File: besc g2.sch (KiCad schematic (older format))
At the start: 7 parts

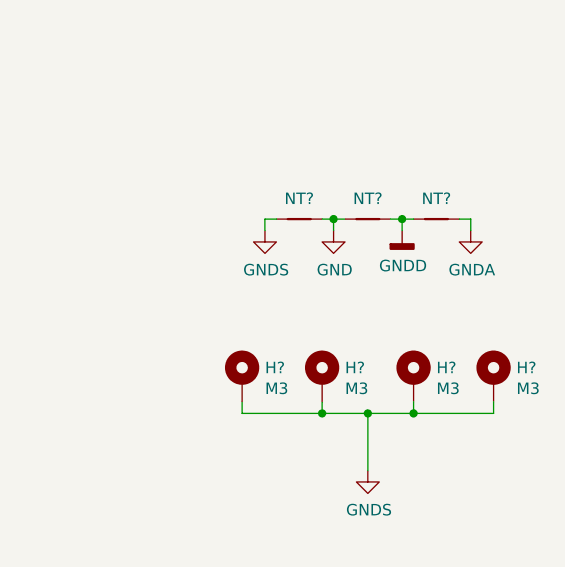
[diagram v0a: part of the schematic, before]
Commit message: power stage layout draft
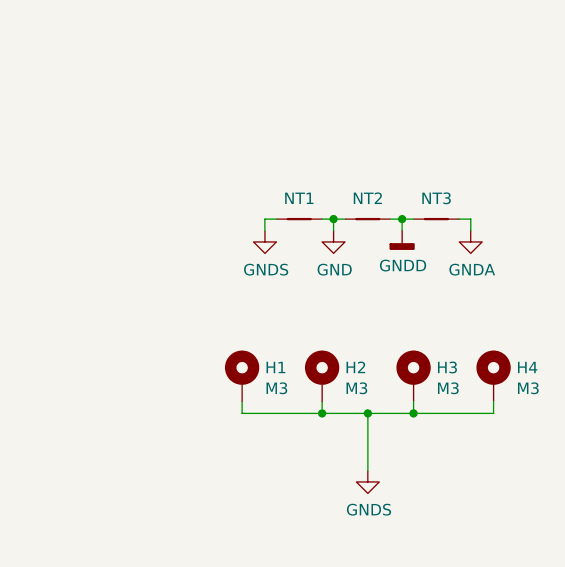
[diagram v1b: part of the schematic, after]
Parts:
- H1, H2, H3, H4: renamed from H?; footprint (none) -> MountingHole:MountingHole_3.2mm_M3_Pad_Via
- NT1, NT2, NT3: renamed from NT?; footprint (none) -> NetTie:NetTie-2_THT_Pad1.0mm
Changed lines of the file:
@@
 P 10150 3350
 AR Path="/5CA11DF8/5CEB744C" Ref="#PWR?"  Part="1"
-AR Path="/5CEB744C" Ref="#PWR0101"  Part="1"
-F 0 "#PWR0101" H 10150 3100 50  0001 C CNN
+AR Path="/5CEB744C" Ref="#PWR05"  Part="1"
+F 0 "#PWR05" H 10150 3100 50  0001 C CNN
 F 1 "GNDA" H 10155 3177 50  0000 C CNN
 F 2 "" H 10150 3350 50  0001 C CNN
@@
 $EndSheet
 $Comp
-L Device:Net-Tie_2 NT?
+L Device:Net-Tie_2 NT2
 U 1 1 5D34A5B5
 P 9700 3300
-F 0 "NT?" H 9700 3389 50  0000 C CNN
+F 0 "NT2" H 9700 3389 50  0000 C CNN
 F 1 "nt" H 9700 3390 50  0001 C CNN
-F 2 "" H 9700 3300 50  0001 C CNN
+F 2 "NetTie:NetTie-2_THT_Pad1.0mm" H 9700 3300 50  0001 C CNN
 F 3 "~" H 9700 3300 50  0001 C CNN
 	1    9700 3300
@@
 $EndComp
 $Comp
-L Device:Net-Tie_2 NT?
+L Device:Net-Tie_2 NT3
 U 1 1 5D34B582
 P 10000 3300
-F 0 "NT?" H 10000 3389 50  0000 C CNN
+F 0 "NT3" H 10000 3389 50  0000 C CNN
 F 1 "nt" H 10000 3390 50  0001 C CNN
-F 2 "" H 10000 3300 50  0001 C CNN
+F 2 "NetTie:NetTie-2_THT_Pad1.0mm" H 10000 3300 50  0001 C CNN
 F 3 "~" H 10000 3300 50  0001 C CNN
 	1    10000 3300
@@
 P 9850 3350
 AR Path="/5CA11DF8/5CEB7446" Ref="#PWR?"  Part="1"
-AR Path="/5CEB7446" Ref="#PWR0102"  Part="1"
-F 0 "#PWR0102" H 9850 3100 50  0001 C CNN
+AR Path="/5CEB7446" Ref="#PWR04"  Part="1"
+F 0 "#PWR04" H 9850 3100 50  0001 C CNN
 F 1 "GNDD" H 9854 3195 50  0000 C CNN
 F 2 "" H 9850 3350 50  0001 C CNN
@@
 P 9550 3350
 AR Path="/5CA11DF8/5CEB7455" Ref="#PWR?"  Part="1"
-AR Path="/5CEB7455" Ref="#PWR0103"  Part="1"
-F 0 "#PWR0103" H 9550 3100 50  0001 C CNN
+AR Path="/5CEB7455" Ref="#PWR02"  Part="1"
+F 0 "#PWR02" H 9550 3100 50  0001 C CNN
 F 1 "GND" H 9555 3177 50  0000 C CNN
 F 2 "" H 9550 3350 50  0001 C CNN
@@
 $EndComp
 $Comp
-L Mechanical:MountingHole_Pad H?
+L Mechanical:MountingHole_Pad H2
 U 1 1 5DC1CF77
 P 9500 4000
-F 0 "H?" H 9600 4049 50  0000 L CNN
+F 0 "H2" H 9600 4049 50  0000 L CNN
 F 1 "M3" H 9600 3958 50  0000 L CNN
-F 2 "" H 9500 4000 50  0001 C CNN
+F 2 "MountingHole:MountingHole_3.2mm_M3_Pad_Via" H 9500 4000 50  0001 C CNN
 F 3 "~" H 9500 4000 50  0001 C CNN
 	1    9500 4000
@@
 $EndComp
 $Comp
-L Mechanical:MountingHole_Pad H?
+L Mechanical:MountingHole_Pad H3
 U 1 1 5DC1D147
 P 9900 4000
-F 0 "H?" H 10000 4049 50  0000 L CNN
+F 0 "H3" H 10000 4049 50  0000 L CNN
 F 1 "M3" H 10000 3958 50  0000 L CNN
-F 2 "" H 9900 4000 50  0001 C CNN
+F 2 "MountingHole:MountingHole_3.2mm_M3_Pad_Via" H 9900 4000 50  0001 C CNN
 F 3 "~" H 9900 4000 50  0001 C CNN
 	1    9900 4000
@@
 $EndComp
 $Comp
-L Mechanical:MountingHole_Pad H?
+L Mechanical:MountingHole_Pad H4
 U 1 1 5DC1D371
 P 10250 4000
-F 0 "H?" H 10350 4049 50  0000 L CNN
+F 0 "H4" H 10350 4049 50  0000 L CNN
 F 1 "M3" H 10350 3958 50  0000 L CNN
-F 2 "" H 10250 4000 50  0001 C CNN
+F 2 "MountingHole:MountingHole_3.2mm_M3_Pad_Via" H 10250 4000 50  0001 C CNN
 F 3 "~" H 10250 4000 50  0001 C CNN
 	1    10250 4000
@@
 	9700 4150 9900 4150
 $Comp
-L power:GNDS #PWR0104
+L power:GNDS #PWR03
 U 1 1 5DC1FB10
 P 9700 4400
-F 0 "#PWR0104" H 9700 4150 50  0001 C CNN
+F 0 "#PWR03" H 9700 4150 50  0001 C CNN
 F 1 "GNDS" H 9705 4227 50  0000 C CNN
 F 2 "" H 9700 4400 50  0001 C CNN
@@
 	9700 4150 9700 4400
 $Comp
-L power:GNDS #PWR0105
+L power:GNDS #PWR01
 U 1 1 5DC2074C
 P 9250 3350
-F 0 "#PWR0105" H 9250 3100 50  0001 C CNN
+F 0 "#PWR01" H 9250 3100 50  0001 C CNN
 F 1 "GNDS" H 9255 3177 50  0000 C CNN
 F 2 "" H 9250 3350 50  0001 C CNN
@@
 $EndComp
 $Comp
-L Device:Net-Tie_2 NT?
+L Device:Net-Tie_2 NT1
 U 1 1 5DC213D0
 P 9400 3300
-F 0 "NT?" H 9400 3389 50  0000 C CNN
+F 0 "NT1" H 9400 3389 50  0000 C CNN
 F 1 "nt" H 9400 3390 50  0001 C CNN
-F 2 "" H 9400 3300 50  0001 C CNN
+F 2 "NetTie:NetTie-2_THT_Pad1.0mm" H 9400 3300 50  0001 C CNN
 F 3 "~" H 9400 3300 50  0001 C CNN
 	1    9400 3300
@@
 	9150 4100 9150 4150
 $Comp
-L Mechanical:MountingHole_Pad H?
+L Mechanical:MountingHole_Pad H1
 U 1 1 5DC1CB14
 P 9150 4000
-F 0 "H?" H 9250 4049 50  0000 L CNN
+F 0 "H1" H 9250 4049 50  0000 L CNN
 F 1 "M3" H 9250 3958 50  0000 L CNN
-F 2 "" H 9150 4000 50  0001 C CNN
+F 2 "MountingHole:MountingHole_3.2mm_M3_Pad_Via" H 9150 4000 50  0001 C CNN
 F 3 "~" H 9150 4000 50  0001 C CNN
 	1    9150 4000

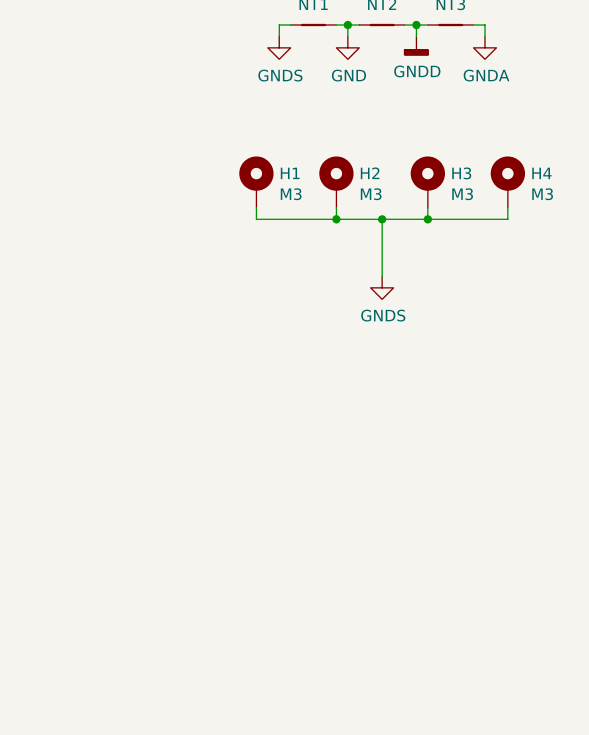
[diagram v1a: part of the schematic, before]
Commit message: isolated drivers, layout
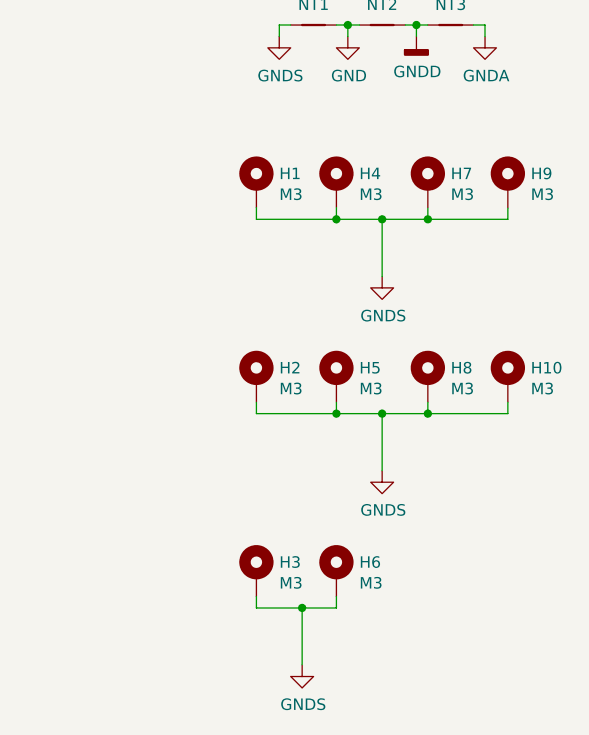
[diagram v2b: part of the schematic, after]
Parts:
- added H10, H2, H3, H5, H6, H8: M3, MountingHole:MountingHole_3.2mm_M3_Pad_Via, symbol Mechanical:MountingHole_Pad
- renumbered H2 to H4, H3 to H7, H4 to H9
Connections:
- net GNDS: now also H10.1, H2.1, H3.1, H5.1, H6.1, H8.1
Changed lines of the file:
@@
 P 10150 3350
 AR Path="/5CA11DF8/5CEB744C" Ref="#PWR?"  Part="1"
-AR Path="/5CEB744C" Ref="#PWR05"  Part="1"
-F 0 "#PWR05" H 10150 3100 50  0001 C CNN
+AR Path="/5CEB744C" Ref="#PWR07"  Part="1"
+F 0 "#PWR07" H 10150 3100 50  0001 C CNN
 F 1 "GNDA" H 10155 3177 50  0000 C CNN
 F 2 "" H 10150 3350 50  0001 C CNN
@@
 P 9850 3350
 AR Path="/5CA11DF8/5CEB7446" Ref="#PWR?"  Part="1"
-AR Path="/5CEB7446" Ref="#PWR04"  Part="1"
-F 0 "#PWR04" H 9850 3100 50  0001 C CNN
+AR Path="/5CEB7446" Ref="#PWR06"  Part="1"
+F 0 "#PWR06" H 9850 3100 50  0001 C CNN
 F 1 "GNDD" H 9854 3195 50  0000 C CNN
 F 2 "" H 9850 3350 50  0001 C CNN
@@
 P 9550 3350
 AR Path="/5CA11DF8/5CEB7455" Ref="#PWR?"  Part="1"
-AR Path="/5CEB7455" Ref="#PWR02"  Part="1"
-F 0 "#PWR02" H 9550 3100 50  0001 C CNN
+AR Path="/5CEB7455" Ref="#PWR03"  Part="1"
+F 0 "#PWR03" H 9550 3100 50  0001 C CNN
 F 1 "GND" H 9555 3177 50  0000 C CNN
 F 2 "" H 9550 3350 50  0001 C CNN
@@
 $EndComp
 $Comp
-L Mechanical:MountingHole_Pad H2
+L Mechanical:MountingHole_Pad H4
 U 1 1 5DC1CF77
 P 9500 4000
-F 0 "H2" H 9600 4049 50  0000 L CNN
+F 0 "H4" H 9600 4049 50  0000 L CNN
 F 1 "M3" H 9600 3958 50  0000 L CNN
 F 2 "MountingHole:MountingHole_3.2mm_M3_Pad_Via" H 9500 4000 50  0001 C CNN
@@
 $EndComp
 $Comp
-L Mechanical:MountingHole_Pad H3
+L Mechanical:MountingHole_Pad H7
 U 1 1 5DC1D147
 P 9900 4000
-F 0 "H3" H 10000 4049 50  0000 L CNN
+F 0 "H7" H 10000 4049 50  0000 L CNN
 F 1 "M3" H 10000 3958 50  0000 L CNN
 F 2 "MountingHole:MountingHole_3.2mm_M3_Pad_Via" H 9900 4000 50  0001 C CNN
@@
 $EndComp
 $Comp
-L Mechanical:MountingHole_Pad H4
+L Mechanical:MountingHole_Pad H9
 U 1 1 5DC1D371
 P 10250 4000
-F 0 "H4" H 10350 4049 50  0000 L CNN
+F 0 "H9" H 10350 4049 50  0000 L CNN
 F 1 "M3" H 10350 3958 50  0000 L CNN
 F 2 "MountingHole:MountingHole_3.2mm_M3_Pad_Via" H 10250 4000 50  0001 C CNN
@@
 	9700 4150 9900 4150
 $Comp
-L power:GNDS #PWR03
+L power:GNDS #PWR04
 U 1 1 5DC1FB10
 P 9700 4400
-F 0 "#PWR03" H 9700 4150 50  0001 C CNN
+F 0 "#PWR04" H 9700 4150 50  0001 C CNN
 F 1 "GNDS" H 9705 4227 50  0000 C CNN
 F 2 "" H 9700 4400 50  0001 C CNN
@@
 	1    0    0    -1
 $EndComp
+$Comp
+L Mechanical:MountingHole_Pad H5
+U 1 1 5CC5498C
+P 9500 4850
+F 0 "H5" H 9600 4899 50  0000 L CNN
+F 1 "M3" H 9600 4808 50  0000 L CNN
+F 2 "MountingHole:MountingHole_3.2mm_M3_Pad_Via" H 9500 4850 50  0001 C CNN
+F 3 "~" H 9500 4850 50  0001 C CNN
+	1    9500 4850
+	1    0    0    -1
+$EndComp
+$Comp
+L Mechanical:MountingHole_Pad H8
+U 1 1 5CC54992
+P 9900 4850
+F 0 "H8" H 10000 4899 50  0000 L CNN
+F 1 "M3" H 10000 4808 50  0000 L CNN
+F 2 "MountingHole:MountingHole_3.2mm_M3_Pad_Via" H 9900 4850 50  0001 C CNN
+F 3 "~" H 9900 4850 50  0001 C CNN
+	1    9900 4850
+	1    0    0    -1
+$EndComp
+$Comp
+L Mechanical:MountingHole_Pad H10
+U 1 1 5CC54998
+P 10250 4850
+F 0 "H10" H 10350 4899 50  0000 L CNN
+F 1 "M3" H 10350 4808 50  0000 L CNN
+F 2 "MountingHole:MountingHole_3.2mm_M3_Pad_Via" H 10250 4850 50  0001 C CNN
+F 3 "~" H 10250 4850 50  0001 C CNN
+	1    10250 4850
+	1    0    0    -1
+$EndComp
+Wire Wire Line
+	9150 5000 9500 5000
+Wire Wire Line
+	10250 5000 10250 4950
+Wire Wire Line
+	9900 4950 9900 5000
+Connection ~ 9900 5000
+Wire Wire Line
+	9900 5000 10250 5000
+Wire Wire Line
+	9500 4950 9500 5000
+Wire Wire Line
+	9500 5000 9700 5000
+Connection ~ 9500 5000
+Connection ~ 9700 5000
+Wire Wire Line
+	9700 5000 9900 5000
+$Comp
+L power:GNDS #PWR05
+U 1 1 5CC549A8
+P 9700 5250
+F 0 "#PWR05" H 9700 5000 50  0001 C CNN
+F 1 "GNDS" H 9705 5077 50  0000 C CNN
+F 2 "" H 9700 5250 50  0001 C CNN
+F 3 "" H 9700 5250 50  0001 C CNN
+	1    9700 5250
+	1    0    0    -1
+$EndComp
+Wire Wire Line
+	9700 5000 9700 5250
+Wire Wire Line
+	9150 4950 9150 5000
+$Comp
+L Mechanical:MountingHole_Pad H2
+U 1 1 5CC549B0
+P 9150 4850
+F 0 "H2" H 9250 4899 50  0000 L CNN
+F 1 "M3" H 9250 4808 50  0000 L CNN
+F 2 "MountingHole:MountingHole_3.2mm_M3_Pad_Via" H 9150 4850 50  0001 C CNN
+F 3 "~" H 9150 4850 50  0001 C CNN
+	1    9150 4850
+	1    0    0    -1
+$EndComp
+$Comp
+L Mechanical:MountingHole_Pad H6
+U 1 1 5CC5725D
+P 9500 5700
+F 0 "H6" H 9600 5749 50  0000 L CNN
+F 1 "M3" H 9600 5658 50  0000 L CNN
+F 2 "MountingHole:MountingHole_3.2mm_M3_Pad_Via" H 9500 5700 50  0001 C CNN
+F 3 "~" H 9500 5700 50  0001 C CNN
+	1    9500 5700
+	1    0    0    -1
+$EndComp
+Wire Wire Line
+	9150 5850 9350 5850
+Wire Wire Line
+	9500 5800 9500 5850
+$Comp
+L power:GNDS #PWR02
+U 1 1 5CC57279
+P 9350 6100
+F 0 "#PWR02" H 9350 5850 50  0001 C CNN
+F 1 "GNDS" H 9355 5927 50  0000 C CNN
+F 2 "" H 9350 6100 50  0001 C CNN
+F 3 "" H 9350 6100 50  0001 C CNN
+	1    9350 6100
+	1    0    0    -1
+$EndComp
+Wire Wire Line
+	9350 5850 9350 6100
+Wire Wire Line
+	9150 5800 9150 5850
+$Comp
+L Mechanical:MountingHole_Pad H3
+U 1 1 5CC57281
+P 9150 5700
+F 0 "H3" H 9250 5749 50  0000 L CNN
+F 1 "M3" H 9250 5658 50  0000 L CNN
+F 2 "MountingHole:MountingHole_3.2mm_M3_Pad_Via" H 9150 5700 50  0001 C CNN
+F 3 "~" H 9150 5700 50  0001 C CNN
+	1    9150 5700
+	1    0    0    -1
+$EndComp
+Connection ~ 9350 5850
+Wire Wire Line
+	9350 5850 9500 5850
 $EndSCHEMATC

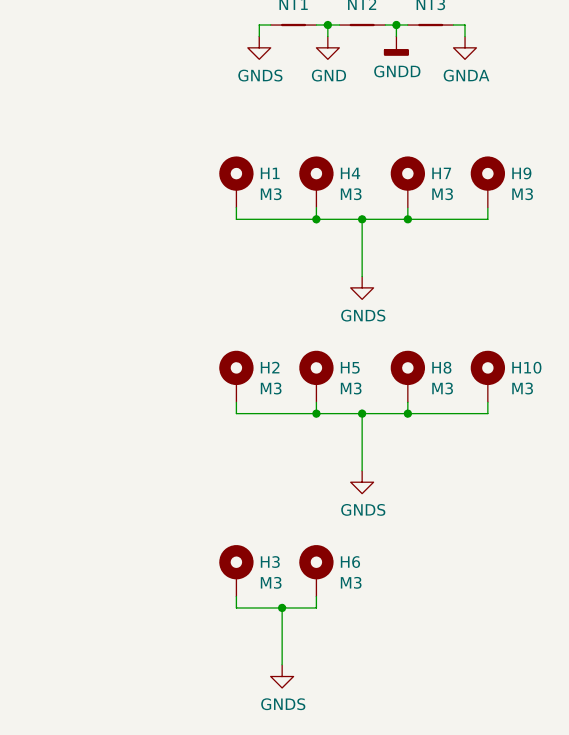
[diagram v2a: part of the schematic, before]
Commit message: 12V PS, isolated gate drivers
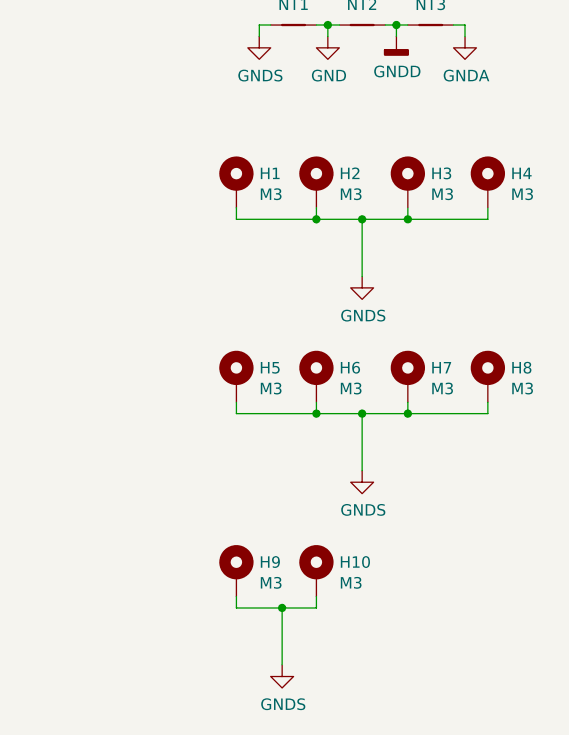
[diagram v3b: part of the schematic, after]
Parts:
- renumbered H6 to H10, H4 to H2, H7 to H3, H9 to H4, H2 to H5, H5 to H6, H8 to H7, H10 to H8, H3 to H9
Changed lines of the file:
@@
 P 10150 3350
 AR Path="/5CA11DF8/5CEB744C" Ref="#PWR?"  Part="1"
-AR Path="/5CEB744C" Ref="#PWR07"  Part="1"
-F 0 "#PWR07" H 10150 3100 50  0001 C CNN
+AR Path="/5CEB744C" Ref="#PWR04"  Part="1"
+F 0 "#PWR04" H 10150 3100 50  0001 C CNN
 F 1 "GNDA" H 10155 3177 50  0000 C CNN
 F 2 "" H 10150 3350 50  0001 C CNN
@@
 P 9850 3350
 AR Path="/5CA11DF8/5CEB7446" Ref="#PWR?"  Part="1"
-AR Path="/5CEB7446" Ref="#PWR06"  Part="1"
-F 0 "#PWR06" H 9850 3100 50  0001 C CNN
+AR Path="/5CEB7446" Ref="#PWR03"  Part="1"
+F 0 "#PWR03" H 9850 3100 50  0001 C CNN
 F 1 "GNDD" H 9854 3195 50  0000 C CNN
 F 2 "" H 9850 3350 50  0001 C CNN
@@
 P 9550 3350
 AR Path="/5CA11DF8/5CEB7455" Ref="#PWR?"  Part="1"
-AR Path="/5CEB7455" Ref="#PWR03"  Part="1"
-F 0 "#PWR03" H 9550 3100 50  0001 C CNN
+AR Path="/5CEB7455" Ref="#PWR02"  Part="1"
+F 0 "#PWR02" H 9550 3100 50  0001 C CNN
 F 1 "GND" H 9555 3177 50  0000 C CNN
 F 2 "" H 9550 3350 50  0001 C CNN
@@
 $EndComp
 $Comp
-L Mechanical:MountingHole_Pad H4
+L Mechanical:MountingHole_Pad H2
 U 1 1 5DC1CF77
 P 9500 4000
-F 0 "H4" H 9600 4049 50  0000 L CNN
+F 0 "H2" H 9600 4049 50  0000 L CNN
 F 1 "M3" H 9600 3958 50  0000 L CNN
 F 2 "MountingHole:MountingHole_3.2mm_M3_Pad_Via" H 9500 4000 50  0001 C CNN
@@
 $EndComp
 $Comp
-L Mechanical:MountingHole_Pad H7
+L Mechanical:MountingHole_Pad H3
 U 1 1 5DC1D147
 P 9900 4000
-F 0 "H7" H 10000 4049 50  0000 L CNN
+F 0 "H3" H 10000 4049 50  0000 L CNN
 F 1 "M3" H 10000 3958 50  0000 L CNN
 F 2 "MountingHole:MountingHole_3.2mm_M3_Pad_Via" H 9900 4000 50  0001 C CNN
@@
 $EndComp
 $Comp
-L Mechanical:MountingHole_Pad H9
+L Mechanical:MountingHole_Pad H4
 U 1 1 5DC1D371
 P 10250 4000
-F 0 "H9" H 10350 4049 50  0000 L CNN
+F 0 "H4" H 10350 4049 50  0000 L CNN
 F 1 "M3" H 10350 3958 50  0000 L CNN
 F 2 "MountingHole:MountingHole_3.2mm_M3_Pad_Via" H 10250 4000 50  0001 C CNN
@@
 	9700 4150 9900 4150
 $Comp
-L power:GNDS #PWR04
+L power:GNDS #PWR05
 U 1 1 5DC1FB10
 P 9700 4400
-F 0 "#PWR04" H 9700 4150 50  0001 C CNN
+F 0 "#PWR05" H 9700 4150 50  0001 C CNN
 F 1 "GNDS" H 9705 4227 50  0000 C CNN
 F 2 "" H 9700 4400 50  0001 C CNN
@@
 $EndComp
 $Comp
-L Mechanical:MountingHole_Pad H5
+L Mechanical:MountingHole_Pad H6
 U 1 1 5CC5498C
 P 9500 4850
-F 0 "H5" H 9600 4899 50  0000 L CNN
+F 0 "H6" H 9600 4899 50  0000 L CNN
 F 1 "M3" H 9600 4808 50  0000 L CNN
 F 2 "MountingHole:MountingHole_3.2mm_M3_Pad_Via" H 9500 4850 50  0001 C CNN
@@
 $EndComp
 $Comp
-L Mechanical:MountingHole_Pad H8
+L Mechanical:MountingHole_Pad H7
 U 1 1 5CC54992
 P 9900 4850
-F 0 "H8" H 10000 4899 50  0000 L CNN
+F 0 "H7" H 10000 4899 50  0000 L CNN
 F 1 "M3" H 10000 4808 50  0000 L CNN
 F 2 "MountingHole:MountingHole_3.2mm_M3_Pad_Via" H 9900 4850 50  0001 C CNN
@@
 $EndComp
 $Comp
-L Mechanical:MountingHole_Pad H10
+L Mechanical:MountingHole_Pad H8
 U 1 1 5CC54998
 P 10250 4850
-F 0 "H10" H 10350 4899 50  0000 L CNN
+F 0 "H8" H 10350 4899 50  0000 L CNN
 F 1 "M3" H 10350 4808 50  0000 L CNN
 F 2 "MountingHole:MountingHole_3.2mm_M3_Pad_Via" H 10250 4850 50  0001 C CNN
@@
 	9700 5000 9900 5000
 $Comp
-L power:GNDS #PWR05
+L power:GNDS #PWR06
 U 1 1 5CC549A8
 P 9700 5250
-F 0 "#PWR05" H 9700 5000 50  0001 C CNN
+F 0 "#PWR06" H 9700 5000 50  0001 C CNN
 F 1 "GNDS" H 9705 5077 50  0000 C CNN
 F 2 "" H 9700 5250 50  0001 C CNN
@@
 	9150 4950 9150 5000
 $Comp
-L Mechanical:MountingHole_Pad H2
+L Mechanical:MountingHole_Pad H5
 U 1 1 5CC549B0
 P 9150 4850
-F 0 "H2" H 9250 4899 50  0000 L CNN
+F 0 "H5" H 9250 4899 50  0000 L CNN
 F 1 "M3" H 9250 4808 50  0000 L CNN
 F 2 "MountingHole:MountingHole_3.2mm_M3_Pad_Via" H 9150 4850 50  0001 C CNN
@@
 $EndComp
 $Comp
-L Mechanical:MountingHole_Pad H6
+L Mechanical:MountingHole_Pad H10
 U 1 1 5CC5725D
 P 9500 5700
-F 0 "H6" H 9600 5749 50  0000 L CNN
+F 0 "H10" H 9600 5749 50  0000 L CNN
 F 1 "M3" H 9600 5658 50  0000 L CNN
 F 2 "MountingHole:MountingHole_3.2mm_M3_Pad_Via" H 9500 5700 50  0001 C CNN
@@
 	9500 5800 9500 5850
 $Comp
-L power:GNDS #PWR02
+L power:GNDS #PWR07
 U 1 1 5CC57279
 P 9350 6100
-F 0 "#PWR02" H 9350 5850 50  0001 C CNN
+F 0 "#PWR07" H 9350 5850 50  0001 C CNN
 F 1 "GNDS" H 9355 5927 50  0000 C CNN
 F 2 "" H 9350 6100 50  0001 C CNN
@@
 	9150 5800 9150 5850
 $Comp
-L Mechanical:MountingHole_Pad H3
+L Mechanical:MountingHole_Pad H9
 U 1 1 5CC57281
 P 9150 5700
-F 0 "H3" H 9250 5749 50  0000 L CNN
+F 0 "H9" H 9250 5749 50  0000 L CNN
 F 1 "M3" H 9250 5658 50  0000 L CNN
 F 2 "MountingHole:MountingHole_3.2mm_M3_Pad_Via" H 9150 5700 50  0001 C CNN

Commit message: layout and routing progress
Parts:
- removed H6: M3, MountingHole:MountingHole_3.2mm_M3_Pad_Via, symbol Mechanical:MountingHole_Pad
- removed NT1, NT2, NT3: nt, NetTie:NetTie-2_THT_Pad1.0mm, symbol Device:Net-Tie_2
- renumbered H5 to H2, H2 to H3, H9 to H4, H7 to H5, H10 to H6, H3 to H7, H4 to H9
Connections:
- net GNDS: no longer H5.1, H6.1, H8.1
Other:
- moved on the sheet: H1, H2, H3, H4, H5, H6, H7, H8, H9

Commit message: finished routing
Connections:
- wire segments 53 -> 52
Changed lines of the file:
@@
 Wire Wire Line
 	3800 4600 4200 4600
-$Comp
-L power:GNDA #PWR?
-U 1 1 5CEB744C
-P 9350 2250
-AR Path="/5CA11DF8/5CEB744C" Ref="#PWR?"  Part="1"
-AR Path="/5CEB744C" Ref="#PWR07"  Part="1"
-F 0 "#PWR07" H 9350 2000 50  0001 C CNN
-F 1 "GNDA" H 9355 2077 50  0000 C CNN
-F 2 "" H 9350 2250 50  0001 C CNN
-F 3 "" H 9350 2250 50  0001 C CNN
-	1    9350 2250
-	1    0    0    -1
-$EndComp
 $Sheet
 S 5950 2800 1050 2150
@@
 $EndComp
 Wire Wire Line
-	8350 3000 8700 3000
-Wire Wire Line
 	9450 3000 9450 2950
 Wire Wire Line
 	9100 2950 9100 3000
-Connection ~ 9100 3000
-Wire Wire Line
-	9100 3000 9450 3000
 Wire Wire Line
 	8700 2950 8700 3000
-Wire Wire Line
-	8700 3000 8900 3000
-Connection ~ 8700 3000
-Connection ~ 8900 3000
-Wire Wire Line
-	8900 3000 9100 3000
 $Comp
 L power:GNDS #PWR03
 U 1 1 5DC1FB10
-P 8900 3250
-F 0 "#PWR03" H 8900 3000 50  0001 C CNN
-F 1 "GNDS" H 8905 3077 50  0000 C CNN
-F 2 "" H 8900 3250 50  0001 C CNN
-F 3 "" H 8900 3250 50  0001 C CNN
-	1    8900 3250
-	1    0    0    -1
-$EndComp
-Wire Wire Line
-	8900 3000 8900 3250
+P 9100 3000
+F 0 "#PWR03" H 9100 2750 50  0001 C CNN
+F 1 "GNDS" H 9105 2827 50  0000 C CNN
+F 2 "" H 9100 3000 50  0001 C CNN
+F 3 "" H 9100 3000 50  0001 C CNN
+	1    9100 3000
+	1    0    0    -1
+$EndComp
 $Comp
 L power:GNDS #PWR01
@@
 $EndComp
 Wire Wire Line
-	8700 4750 8900 4750
-Wire Wire Line
 	9050 4700 9050 4750
-$Comp
-L power:GNDS #PWR05
-U 1 1 5CC57279
-P 8900 5000
-F 0 "#PWR05" H 8900 4750 50  0001 C CNN
-F 1 "GNDS" H 8905 4827 50  0000 C CNN
-F 2 "" H 8900 5000 50  0001 C CNN
-F 3 "" H 8900 5000 50  0001 C CNN
-	1    8900 5000
-	1    0    0    -1
-$EndComp
-Wire Wire Line
-	8900 4750 8900 5000
 Wire Wire Line
 	8700 4700 8700 4750
@@
 	1    0    0    -1
 $EndComp
-Connection ~ 8900 4750
-Wire Wire Line
-	8900 4750 9050 4750
 Wire Wire Line
 	7000 2400 7150 2400
@@
 Wire Wire Line
 	7150 2900 7000 2900
+$Comp
+L power:GNDA #PWR?
+U 1 1 5CEB744C
+P 9350 2250
+AR Path="/5CA11DF8/5CEB744C" Ref="#PWR?"  Part="1"
+AR Path="/5CEB744C" Ref="#PWR07"  Part="1"
+F 0 "#PWR07" H 9350 2000 50  0001 C CNN
+F 1 "GNDA" H 9355 2077 50  0000 C CNN
+F 2 "" H 9350 2250 50  0001 C CNN
+F 3 "" H 9350 2250 50  0001 C CNN
+	1    9350 2250
+	1    0    0    -1
+$EndComp
+Wire Wire Line
+	9350 2250 9350 2150
+Wire Wire Line
+	9350 2150 9050 2150
+Wire Wire Line
+	8750 2150 8750 2250
+Wire Wire Line
+	9050 2250 9050 2150
+Connection ~ 9050 2150
+Wire Wire Line
+	9050 2150 8750 2150
+Wire Wire Line
+	8450 2250 8450 2150
+Wire Wire Line
+	8450 2150 8750 2150
+Connection ~ 8750 2150
 $EndSCHEMATC
